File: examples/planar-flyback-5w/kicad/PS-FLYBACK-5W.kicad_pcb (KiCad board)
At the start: 6 copper layers, 50 x 104 mm, 26 parts, among them J1 18-36 V DC, J2 5 V / 1 A isolated, T1 PLANAR 4:2 / Lm 12uH, U1 LT8302ES8E#PBF

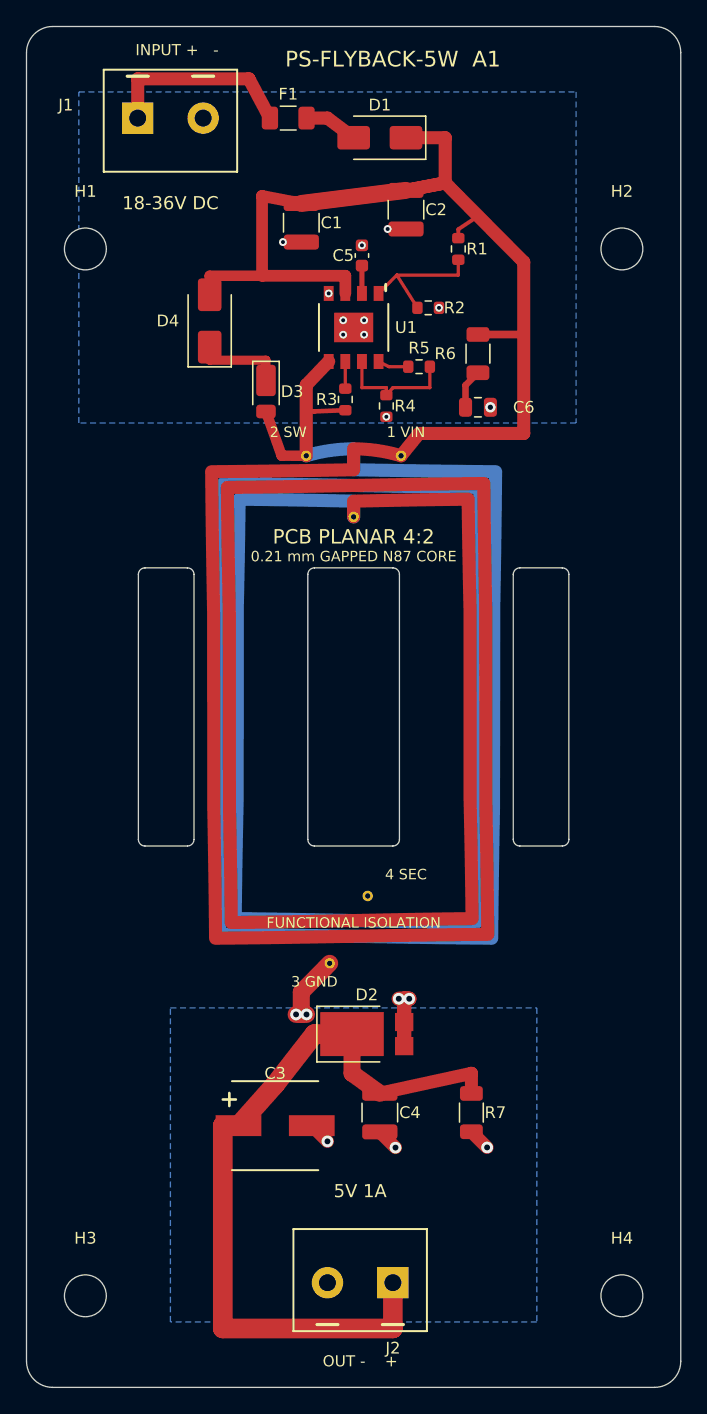
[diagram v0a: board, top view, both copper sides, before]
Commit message: Rework flyback PCB placement and complete KiStack layout audit
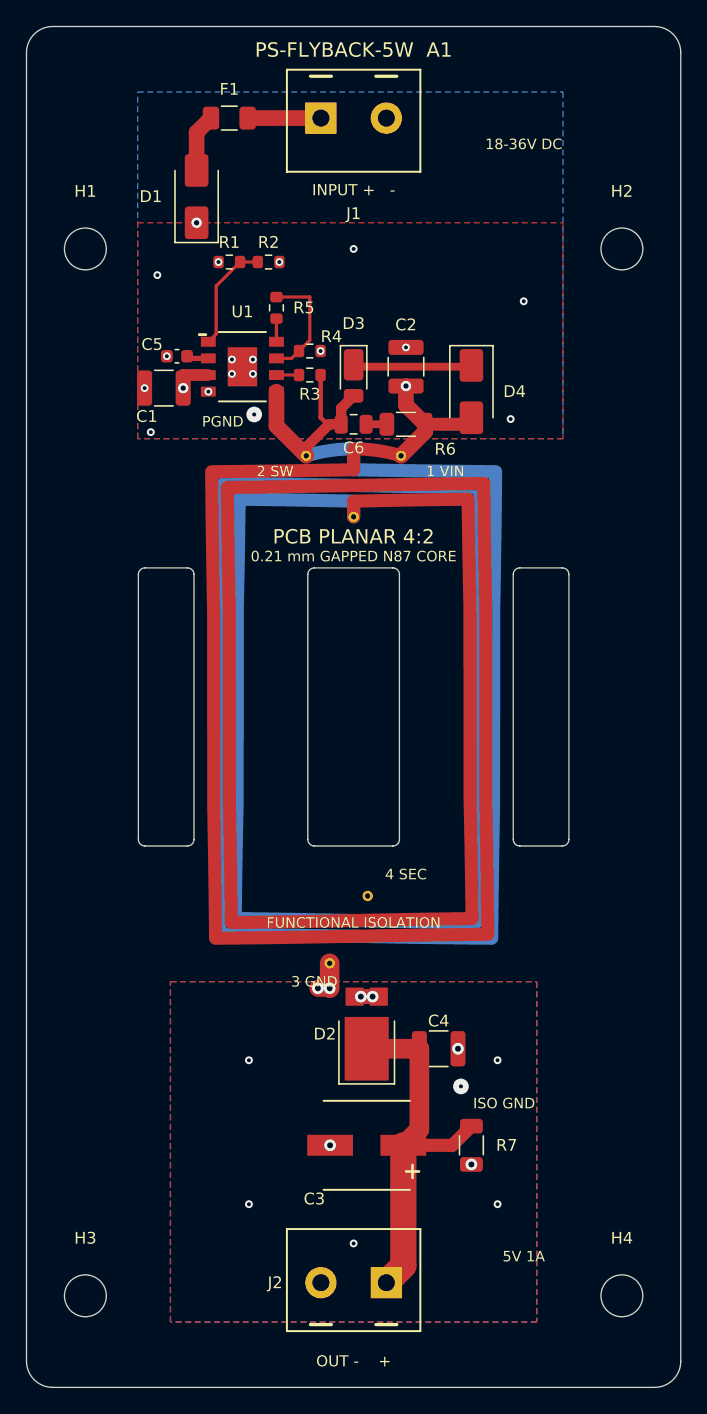
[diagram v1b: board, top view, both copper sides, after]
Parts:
- moved D4 20.7 mm to (109.0, 60.9), turned to -90 degrees
- moved R1 17.5 mm to (90.5, 51.0), turned to 0 degrees
- moved C1 16.4 mm to (85.5, 60.6), turned to 180 degrees
- moved C5 16.1 mm to (86.5, 58.2), turned to 180 degrees
- moved D1 14.7 mm to (88.0, 46.0), turned to 90 degrees
- moved J1 14.0 mm to (97.5, 40.0)
- moved R2 12.7 mm to (93.5, 51.0)
- moved C2 12.0 mm to (104.0, 59.0), turned to 90 degrees
- moved R5 11.8 mm to (94.1, 54.5), turned to 90 degrees
- moved C6 9.59 mm to (100.0, 63.4), turned to 180 degrees
- moved U1 9.01 mm to (91.5, 59.0), turned to 0 degrees
- moved R6 7.71 mm to (104.0, 63.4), turned to 180 degrees
- moved R4 7.20 mm to (96.7, 57.8), turned to 0 degrees
- moved C3 7.16 mm to (101.0, 118.5), turned to 180 degrees
- moved D3 6.81 mm to (100.0, 59.7)
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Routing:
- net /VIN: track 80.7 -> 49.0 mm, vias 0 -> 4
- net /+5V_ISO: track 59.5 -> 28.8 mm
- net /SW: track 34.1 -> 16.6 mm, vias 1 -> 0
- net /VIN_RAW: track 14.9 -> 5.60 mm
- net /GND_ISO: track 10.7 -> 2.81 mm, vias 5 -> 11
- net /SEC_A: track 13.8 -> 9.56 mm
- net /PGND: track 2.80 -> 0.00 mm, vias 10 -> 16
- net /UVLO: track 10.8 -> 8.45 mm
- net /CLAMP: track 6.85 -> 9.10 mm
- net /SNUB: track 3.03 -> 1.59 mm
- net /RREF: track 9.63 -> 8.97 mm
- net /TC: track 2.36 -> 1.77 mm
- added copper zone on F.Cu, net /GND_ISO
- added copper zone on F.Cu, net /PGND
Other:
- board text added: "ISO GND"
- board text added: "PGND"

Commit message: Use American Embedded M3 Edge mounting footprints
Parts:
- H1, H2, H3, H4: footprint amemb-MountingHole:MountingHole_3.2mm_M3_ExposedSubstrate -> amemb-MountingHole:MountingHole_3.2mm_M3_ExposedSubstrate_Edge
- turned H1 to 180 degrees
- turned H3 to 180 degrees

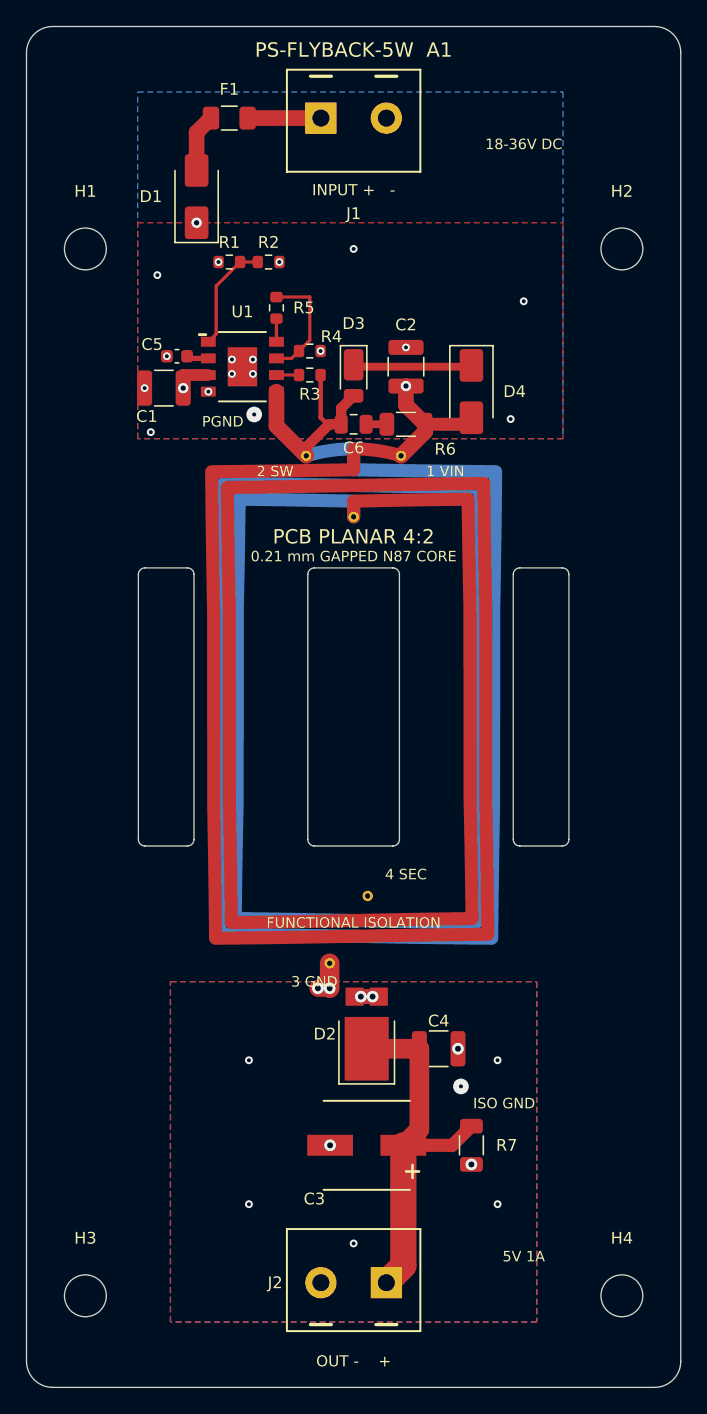
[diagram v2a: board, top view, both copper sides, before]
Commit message: Audit flyback components and improve filtering and ground stitching
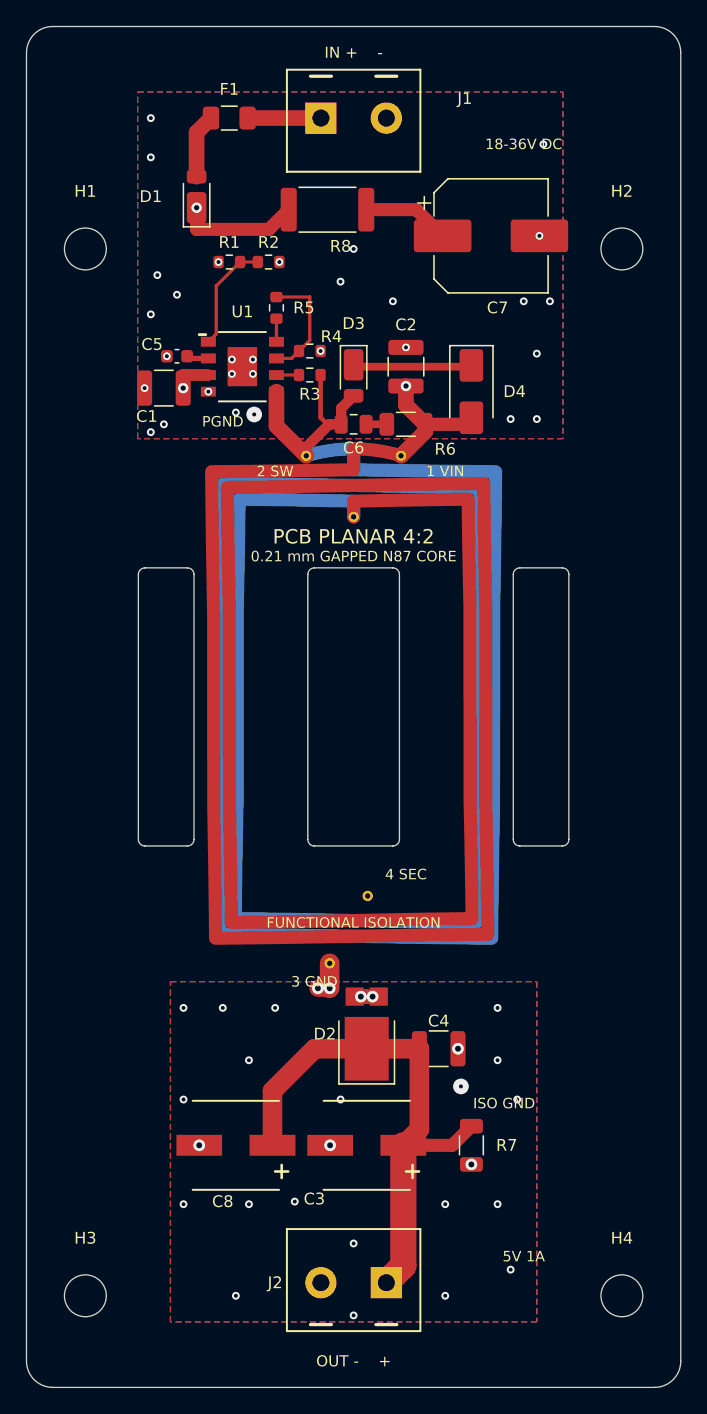
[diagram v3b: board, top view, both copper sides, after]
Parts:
- added C7: 47u / 63 V, Flyback:CP_Elec_8x10.5, F.Cu at (110.5, 49.0)
- added C8: 180u 16V, Flyback:CP_Panasonic_C6, F.Cu at (91.0, 118.5)
- added R8: 2.2R 1.5 W, Flyback:R_2512_6332Metric, F.Cu at (98.0, 47.0)
- C1, C2: value 10u / 50 V X7R -> 10u 50V X7R
- C3: value 180u / 16 V polymer -> 180u 16V
- C4: value 22u / 16 V -> 22u 16V X7R
- C6: value 470p / 100 V C0G -> 470p / 450 V C0G
- D1: value SS110 -> DFLS1100-7; footprint Flyback:D_SMA -> Flyback:D_PowerDI-123
- D4: value SMAJ13A-13-F -> SMAJ12A-13-F
- R1: value 681k 1% -> 649k 1%
- R6: value 39R 0.667 W -> 39R 0.66 W
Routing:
- net /+5V_ISO: track 28.8 -> 41.4 mm
- net /VIN: track 49.0 -> 59.4 mm
- net /VIN_DAMP: track 0.00 -> 6.67 mm
- net /PGND: vias 16 -> 29
- net /GND_ISO: vias 11 -> 26
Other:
- board text added: "IN + -"
- board text removed: "INPUT + -"
- board text removed: "PS-FLYBACK-5W A1"

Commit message: Move flyback mounting holes to corners for capacitor clearance
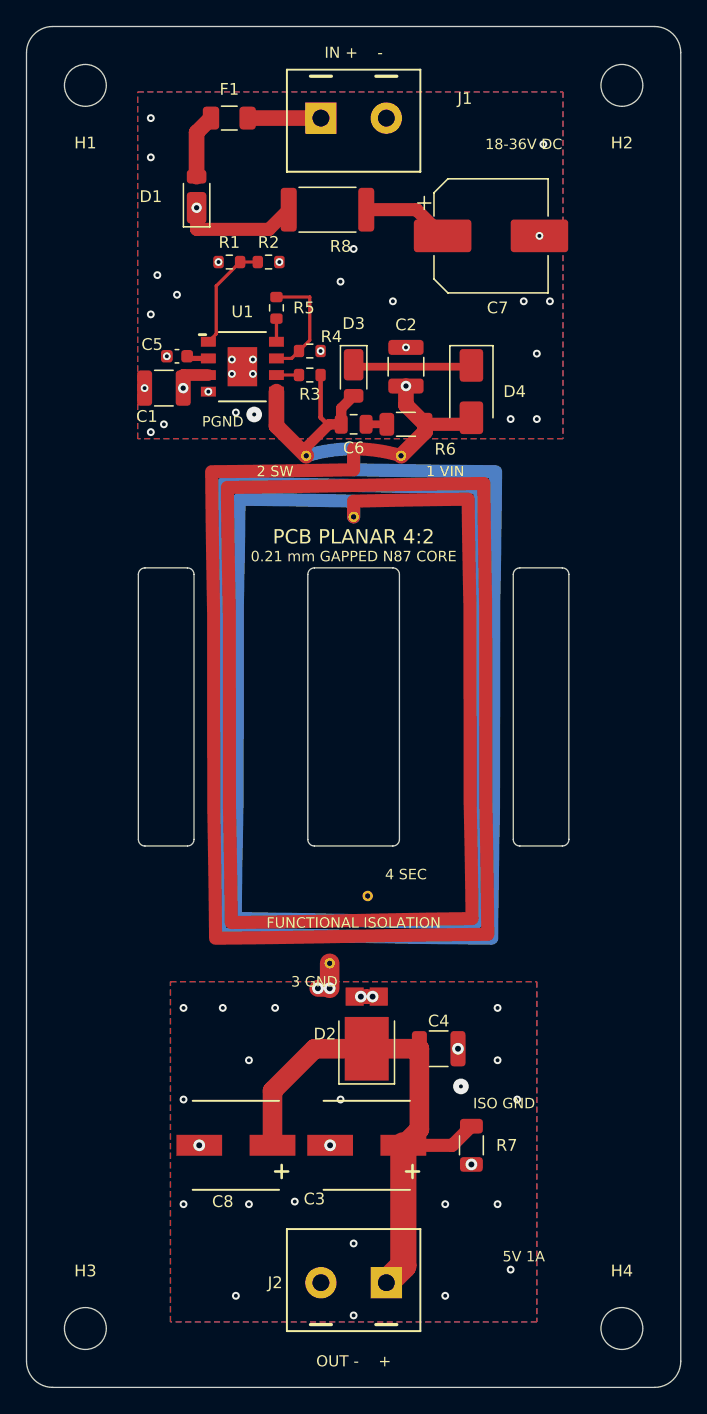
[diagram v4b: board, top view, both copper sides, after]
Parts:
- moved H1 12.5 mm to (79.5, 37.5)
- moved H2 12.5 mm to (120.5, 37.5)
- moved H3 2.50 mm to (79.5, 132.5)
- moved H4 2.50 mm to (120.5, 132.5)

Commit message: Replace flyback fuse and feedback resistor with stocked JLCPCB parts (#13)
* Replace flyback fuse and correct sourcing scope and 3D model

* Document turnkey blockers and five-board manufacturing budget

* Replace R3 with stocked Vishay precision resistor
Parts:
- F1: value 1 A / 63 V fast -> 1 A / 63 V DC fast; footprint Flyback:Fuse_1206_3216Metric -> Flyback:Fuse_Bourns_SF1206F

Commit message: Prepare stocked flyback BOM and JLCPCB manufacturing review panel (#14)
* Improve flyback feedback-current margin and prototype clamp budget

* Prepare stocked flyback BOM and JLCPCB assembly review panel

* Normalize generated panel rule file and refresh package integrity
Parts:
- C6: value 470p / 450 V C0G -> 470p / 100 V C0G
- R3: value 106k 0.1% -> 113k 0.1%
- R4: value 10k 0.1% -> 10.7k 0.1%
- R5: value 118k 1% -> 127k 0.1%
- R6: value 39R 0.66 W -> 39R 0.75 W
- R8: value 2.2R 1.5 W -> 2.2R 2 W; footprint Flyback:R_2512_6332Metric -> Flyback:R_Bourns_CRM2512
- U1: value LT8302ES8E#PBF -> LT8302IS8E#PBF

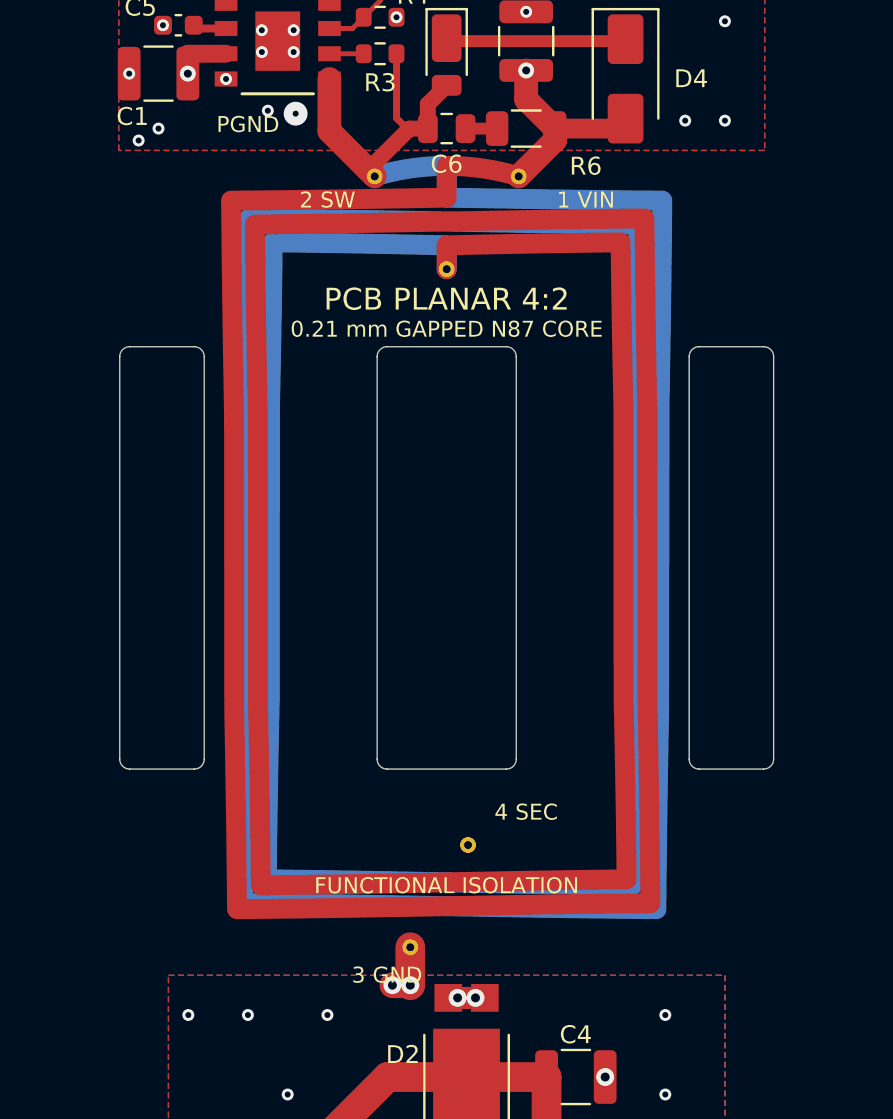
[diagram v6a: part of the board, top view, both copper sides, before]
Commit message: Add flyback A2 with stocked factory-gapped ELP22 cores
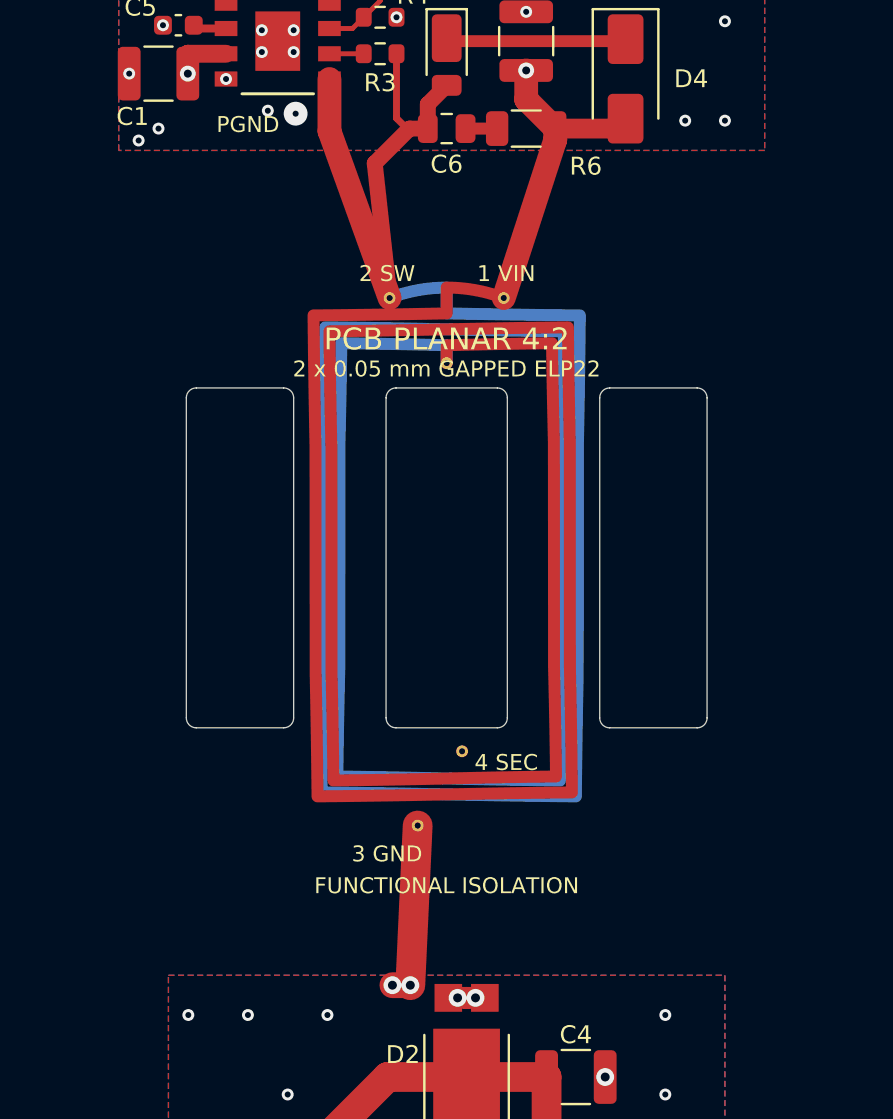
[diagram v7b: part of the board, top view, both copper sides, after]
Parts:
- T1: value PLANAR 4:2 / Lm 12uH -> PLANAR 4:2 / Lm 13.12uH; footprint Flyback:Planar_EELP32_4T_2T -> Flyback:Planar_EELP22_4T_2T
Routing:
- net /SW: track 16.6 -> 28.4 mm
- net /GND_ISO: track 2.81 -> 8.94 mm
- net /VIN: track 59.8 -> 65.6 mm
- net /SEC_A: track 9.56 -> 14.3 mm
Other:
- outline, holes or cut-outs redrawn
- board text added: "2 x 0.05 mm GAPPED ELP22"
- board text added: "A2 ENGINEERING PROTOTYPE"
- board text removed: "0.21 mm GAPPED N87 CORE"
- board text removed: "A1 ENGINEERING PROTOTYPE"
